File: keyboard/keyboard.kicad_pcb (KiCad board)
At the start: 2 copper layers, 64 parts, among them J1 Conn_01x04, J2 Conn_01x04, SW1 SW_Push, SW10 SW_Push, SW11 SW_Push, SW12 SW_Push, SW13 SW_Push, SW14 SW_Push, SW15 SW_Push, SW16 SW_Push, SW17 SW_Push, SW18 SW_Push, SW19 SW_Push, SW2 SW_Push, SW20 SW_Push, SW21 SW_Push, SW3 SW_Push, SW4 SW_Push, SW5 SW_Push, SW6 SW_Push, SW7 SW_Push, SW8 SW_Push, SW9 SW_Push, U1 AP2127K-3.3, U2 USBLC6-2SC6, U3 STM32F072CBTx

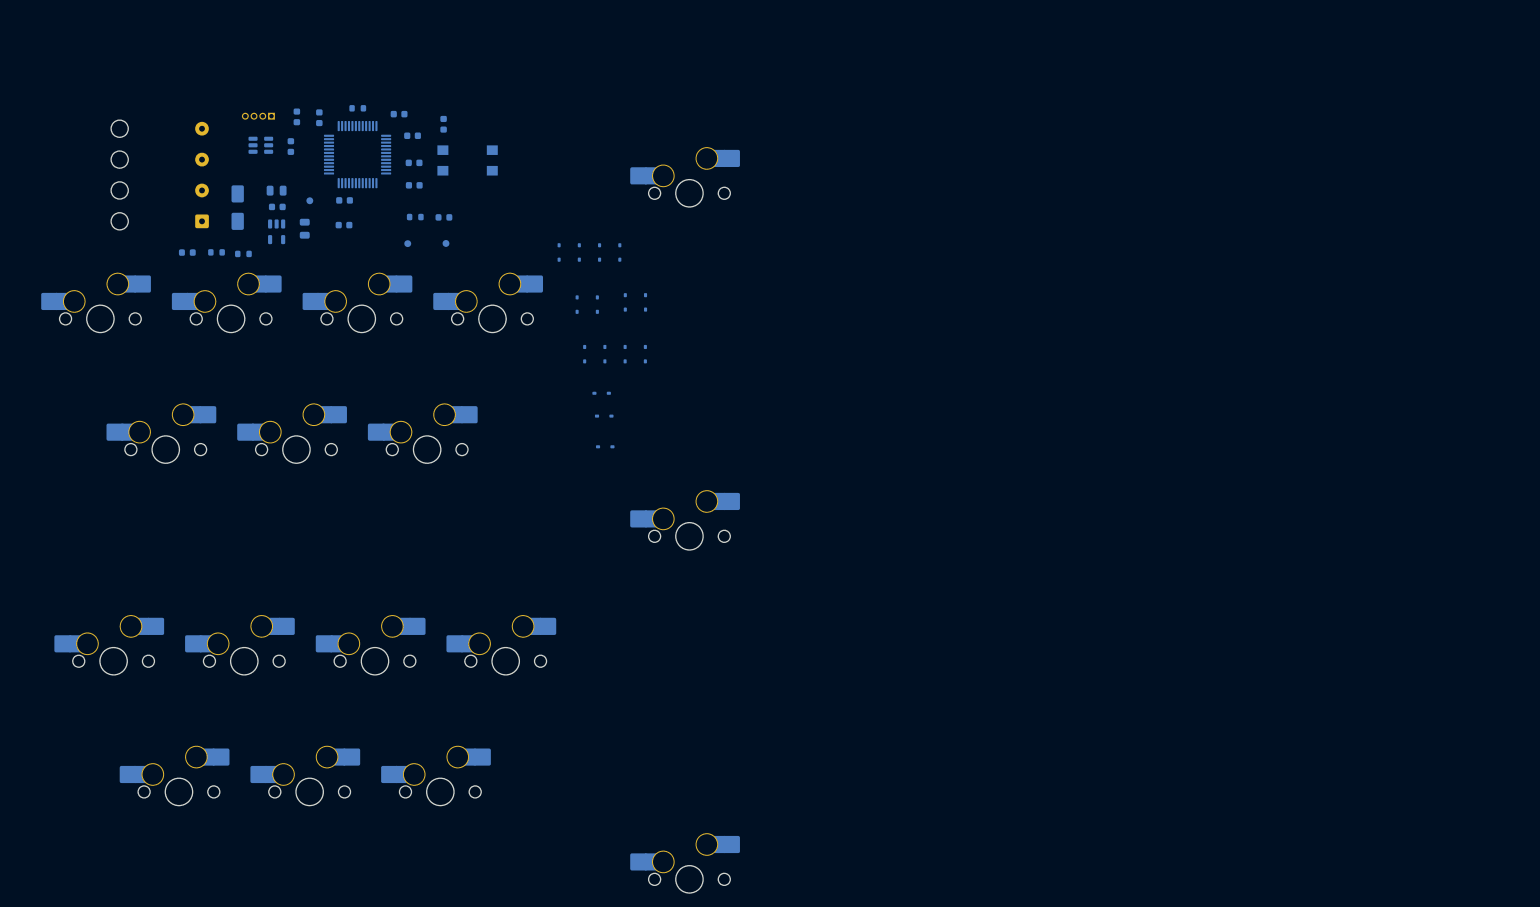
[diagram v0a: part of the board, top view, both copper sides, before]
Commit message: Key layout according to TB drawing.
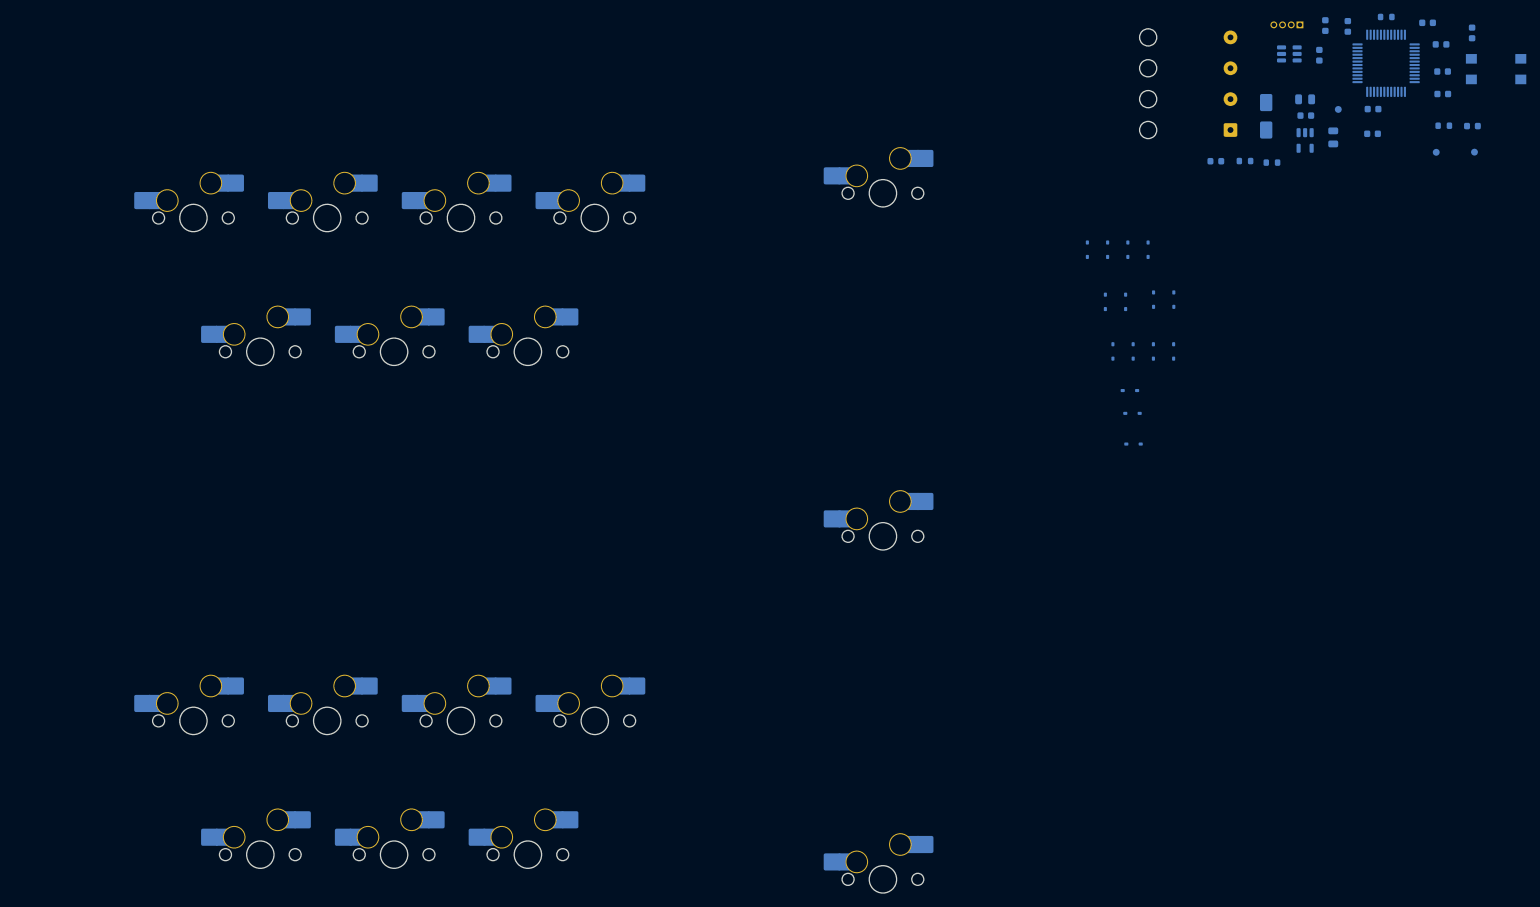
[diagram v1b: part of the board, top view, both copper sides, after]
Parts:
- moved C1 150.5 mm to (248.1, 24.9)
- moved C11 150.5 mm to (266.1, 30.5)
- moved C13 150.5 mm to (249.0, 20.6)
- moved C6 150.5 mm to (265.9, 23.3)
- moved C9 150.5 mm to (255.9, 36.3)
- moved D1 150.5 mm to (240.4, 33.8)
- moved D2 150.5 mm to (233.0, 40.3)
- moved D3 150.5 mm to (270.4, 35.2)
- moved R2 150.5 mm to (237.3, 40.3)
- moved R4 150.5 mm to (257.9, 19.3)
- moved TP1 150.5 mm to (270.7, 39.0)
- moved U2 150.5 mm to (243.7, 24.7)
- moved C10 150.5 mm to (266.1, 27.2)
- moved C12 150.5 mm to (252.3, 20.7)
- moved C2 150.5 mm to (246.0, 31.3)
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
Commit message: Added board outlines 12mm from key switch centres.
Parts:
- moved C1 149.2 mm to (114.0, 90.1)
- moved C11 149.2 mm to (131.9, 95.8)
- moved C13 149.2 mm to (114.8, 85.8)
- moved C6 149.2 mm to (131.7, 88.5)
- moved C9 149.2 mm to (121.7, 101.5)
- moved D1 149.2 mm to (106.2, 99.0)
- moved D2 149.2 mm to (98.9, 105.5)
- moved D3 149.2 mm to (136.3, 100.4)
- moved R2 149.2 mm to (103.1, 105.5)
- moved R4 149.2 mm to (123.7, 84.5)
- moved TP1 149.2 mm to (136.6, 104.2)
- moved U2 149.2 mm to (109.6, 89.9)
- moved C10 149.2 mm to (131.9, 92.5)
- moved C12 149.2 mm to (118.1, 85.9)
- moved C2 149.2 mm to (111.9, 96.5)
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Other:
- board outline added: 166.5 x 124 mm

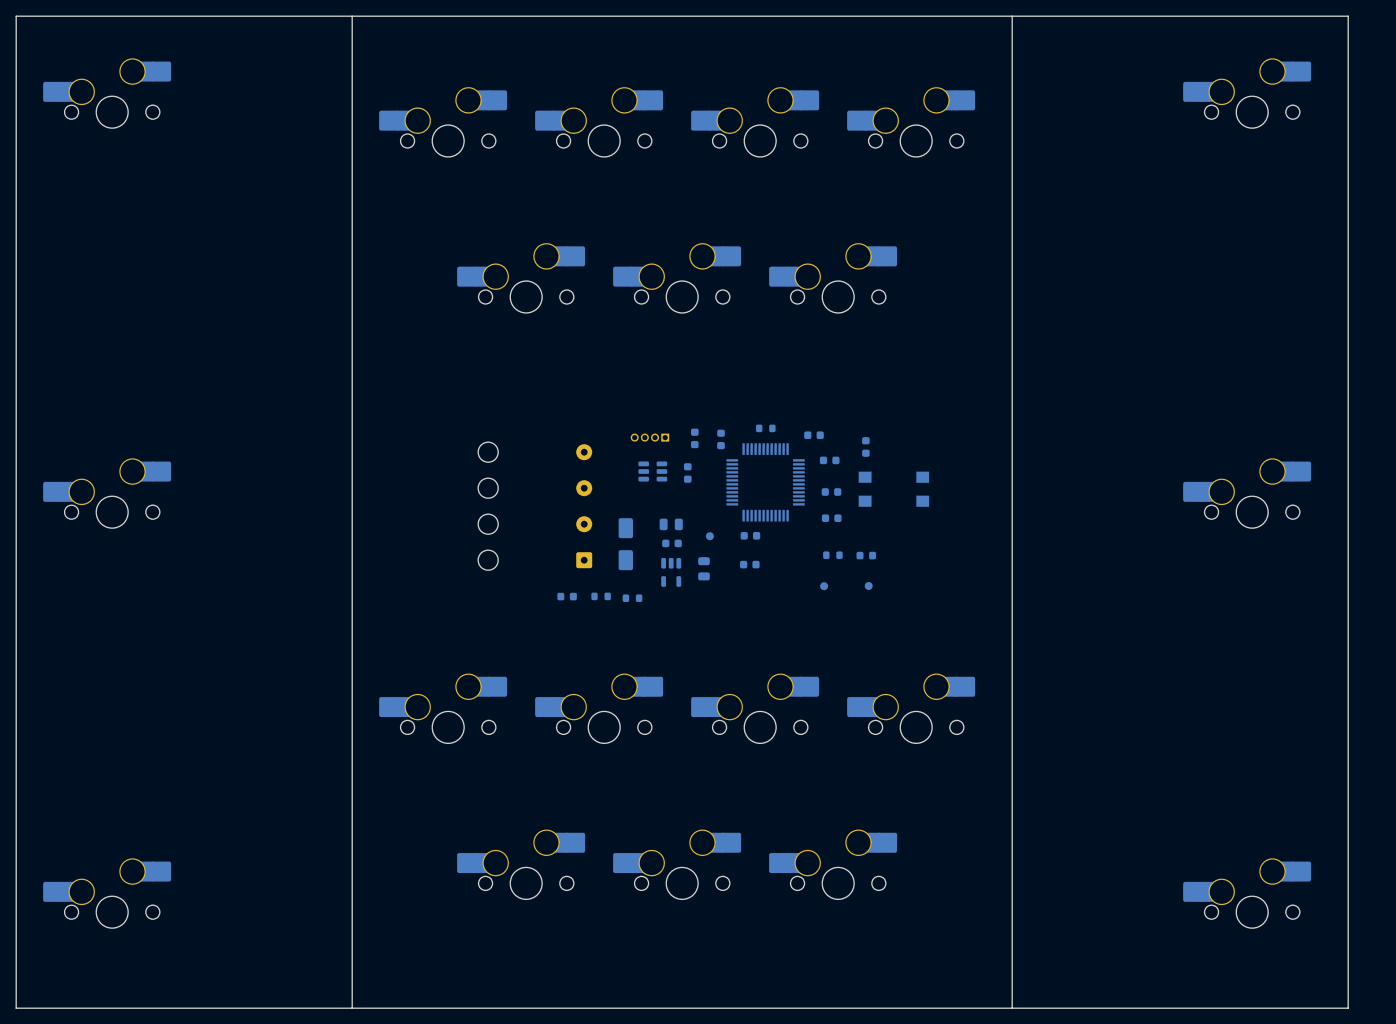
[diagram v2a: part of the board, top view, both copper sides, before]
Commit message: Added connector cutout and V-groove for cut. Moved dimensions onto user drawings layer.
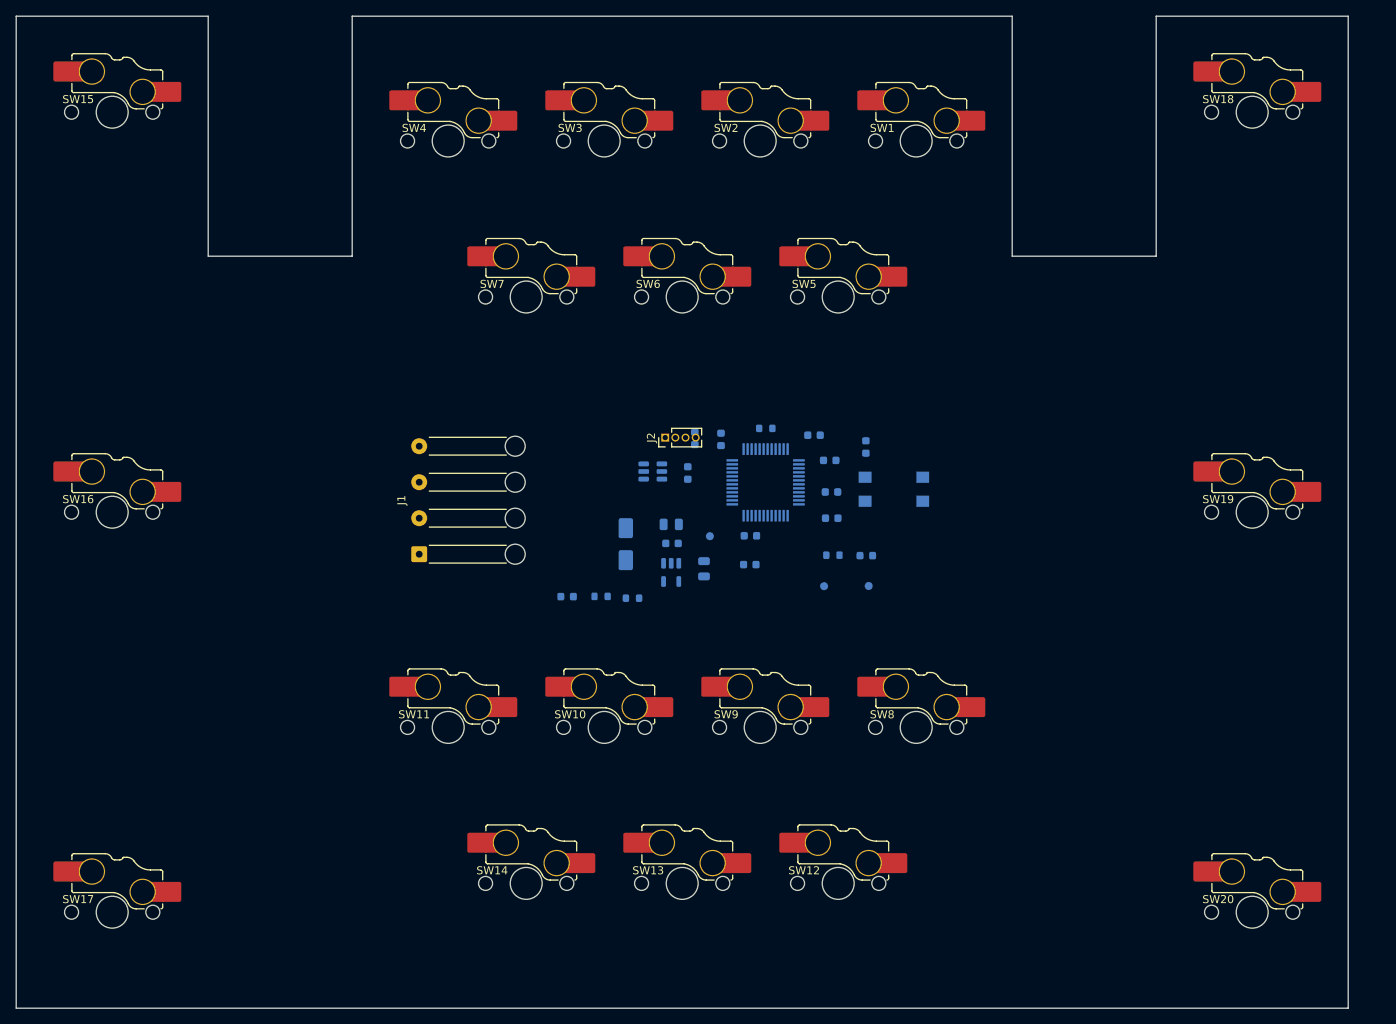
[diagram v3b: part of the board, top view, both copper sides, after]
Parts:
- J1, J2, SW1, SW10, SW11, SW12, SW13, SW14, SW15, SW16, SW17, SW18, SW19, SW2, SW20, SW3, SW4, SW5, SW6, SW7, SW8, SW9: moved to F.Cu
- moved J1 20.6 mm to (80.4, 100.2)
- turned SW1 to 0 degrees
- turned SW10 to 0 degrees
- turned SW11 to 0 degrees
- turned SW12 to 0 degrees
- turned SW13 to 0 degrees
- turned SW14 to 0 degrees
- turned SW15 to 0 degrees
- turned SW16 to 0 degrees
- turned SW17 to 0 degrees
- turned SW18 to 0 degrees
- turned SW19 to 0 degrees
- turned SW2 to 0 degrees
- turned SW20 to 0 degrees
- turned SW3 to 0 degrees
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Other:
- outline, holes or cut-outs redrawn

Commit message: Some mounting holes.
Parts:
- added REF**: MountingHole_2.2mm_M2, MountingHole:MountingHole_2.2mm_M2, F.Cu at (159.5, 152.0)
- added REF**: MountingHole_2.2mm_M2, MountingHole:MountingHole_2.2mm_M2, F.Cu at (67.0, 68.0)
- added REF**: MountingHole_2.2mm_M2, MountingHole:MountingHole_2.2mm_M2, F.Cu at (193.5, 36.0)
- added REF**: MountingHole_2.2mm_M2, MountingHole:MountingHole_2.2mm_M2, F.Cu at (77.0, 38.0)
- added REF**: MountingHole_2.2mm_M2, MountingHole:MountingHole_2.2mm_M2, F.Cu at (159.5, 68.0)
- added REF**: MountingHole_2.2mm_M2, MountingHole:MountingHole_2.2mm_M2, F.Cu at (77.0, 152.0)
- added REF**: MountingHole_2.2mm_M2, MountingHole:MountingHole_2.2mm_M2, F.Cu at (67.0, 152.0)
- added REF**: MountingHole_2.2mm_M2, MountingHole:MountingHole_2.2mm_M2, F.Cu at (159.5, 110.0)
- added REF**: MountingHole_2.2mm_M2, MountingHole:MountingHole_2.2mm_M2, F.Cu at (149.5, 68.0)
- added REF**: MountingHole_2.2mm_M2, MountingHole:MountingHole_2.2mm_M2, F.Cu at (77.0, 110.0)
- added REF**: MountingHole_2.2mm_M2, MountingHole:MountingHole_2.2mm_M2, F.Cu at (193.5, 154.0)
- added REF**: MountingHole_2.2mm_M2, MountingHole:MountingHole_2.2mm_M2, F.Cu at (149.5, 152.0)
- added REF**: MountingHole_2.2mm_M2, MountingHole:MountingHole_2.2mm_M2, F.Cu at (33.0, 36.0)
- added REF**: MountingHole_2.2mm_M2, MountingHole:MountingHole_2.2mm_M2, F.Cu at (149.5, 38.0)
- added REF**: MountingHole_2.2mm_M2, MountingHole:MountingHole_2.2mm_M2, F.Cu at (67.0, 110.0)
- added REF**: MountingHole_2.2mm_M2, MountingHole:MountingHole_2.2mm_M2, F.Cu at (33.0, 154.0)
- added REF**: MountingHole_2.2mm_M2, MountingHole:MountingHole_2.2mm_M2, F.Cu at (149.5, 110.0)
- added REF**: MountingHole_2.2mm_M2, MountingHole:MountingHole_2.2mm_M2, F.Cu at (77.0, 68.0)
- J1, J2: moved to B.Cu
- moved J1 15.3 mm to (95.6, 101.2)
- moved J2 4.18 mm to (107.0, 85.0), turned to -90 degrees

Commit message: Some switch traces.
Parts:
- SW1, SW10, SW11, SW12, SW13, SW14, SW15, SW16, SW17, SW18, SW19, SW2, SW20, SW3, SW4, SW5, SW6, SW7, SW8, SW9: moved to B.Cu
- moved D14 127.6 mm to (111.5, 128.5), turned to 90 degrees
- moved D17 122.1 mm to (121.5, 148.0), turned to 90 degrees
- moved D16 108.8 mm to (141.0, 148.0), turned to 90 degrees
- moved D13 108.4 mm to (131.0, 128.5), turned to 90 degrees
- moved D7 105.0 mm to (119.0, 40.0)
- moved D15 103.9 mm to (160.5, 148.0), turned to 90 degrees
- moved D10 102.4 mm to (121.5, 60.5)
- moved D18 98.7 mm to (127.5, 113.0), turned to 90 degrees
- moved D12 90.6 mm to (150.5, 128.5), turned to 90 degrees
- moved D6 90.2 mm to (131.0, 40.0)
- moved D11 88.7 mm to (170.0, 128.5), turned to 90 degrees
- moved D9 78.9 mm to (141.0, 60.5)
- moved D5 68.0 mm to (150.5, 40.0)
- moved D8 56.4 mm to (160.5, 60.5)
- moved D4 46.2 mm to (170.0, 40.0)
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- renumbered REF** to ?
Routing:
- net Net-(D18-A): track 0.00 -> 235.2 mm, vias 0 -> 1
- net /COL3: track 0.00 -> 226.0 mm, vias 0 -> 1
- net /ROW2: track 0.00 -> 81.7 mm
- net /COL1: track 0.00 -> 56.8 mm, vias 0 -> 5
- net /ROW3: track 0.00 -> 54.6 mm
- net /ROW1: track 0.00 -> 54.4 mm
- net /ROW0: track 0.00 -> 51.0 mm
- net /COL0: track 0.00 -> 50.2 mm, vias 0 -> 3
- net /COL2: track 0.00 -> 29.0 mm, vias 0 -> 3
- net Net-(D7-A): track 0.00 -> 11.0 mm
- net Net-(D6-A): track 0.00 -> 7.07 mm
- net Net-(D5-A): track 0.00 -> 7.07 mm
- net Net-(D4-A): track 0.00 -> 7.07 mm
- net Net-(D14-A): track 0.00 -> 6.15 mm
- net Net-(D13-A): track 0.00 -> 6.15 mm
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
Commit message: Some routing.
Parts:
- removed the ? at (194.5, 154.0)
- removed the ? at (102.0, 70.0)
- removed the ? at (228.5, 38.0)
- removed the ? at (194.5, 70.0)
- removed the ? at (102.0, 154.0)
- removed the ? at (194.5, 112.0)
- removed the ? at (184.5, 70.0)
- removed the ? at (228.5, 156.0)
- removed the ? at (102.0, 112.0)
- removed the ? at (112.0, 70.0)
- removed J1: Conn_01x04, Connector_Wire:SolderWire-0.25sqmm_1x04_P4.5mm_D0.65mm_OD2mm_Relief
- removed SW18, SW19, SW20: SW_Push, PCM_marbastlib-mx:SW_MX_HS_KS-2P02B01-01_1.5u
- added +5V: SolderWirePad_1x01_SMD_1.5x3mm, Connector_Wire:SolderWirePad_1x01_SMD_1.5x3mm, B.Cu at (139.0, 92.5)
- added ?: MountingHole_2.2mm_M2, MountingHole:MountingHole_2.2mm_M2, F.Cu at (128.2, 93.5)
- added ?: MountingHole_2.2mm_M2, MountingHole:MountingHole_2.2mm_M2, F.Cu at (128.2, 89.2)
- added ?: MountingHole_2.2mm_M2, MountingHole:MountingHole_2.2mm_M2, F.Cu at (98.5, 109.2)
- added ?: MountingHole_2.2mm_M2, MountingHole:MountingHole_2.2mm_M2, F.Cu at (104.0, 38.0)
- added ?: MountingHole_2.2mm_M2, MountingHole:MountingHole_2.2mm_M2, F.Cu at (98.5, 113.5)
- added ?: MountingHole_2.2mm_M2, MountingHole:MountingHole_2.2mm_M2, F.Cu at (104.0, 156.0)
- added ?: MountingHole_2.2mm_M2, MountingHole:MountingHole_2.2mm_M2, F.Cu at (128.2, 103.2)
- added ?: MountingHole_2.2mm_M2, MountingHole:MountingHole_2.2mm_M2, F.Cu at (128.2, 99.0)
- added COL3: SolderWirePad_1x01_SMD_1.5x3mm, Connector_Wire:SolderWirePad_1x01_SMD_1.5x3mm, B.Cu at (90.5, 110.2)
- added COL3: SolderWirePad_1x01_SMD_1.5x3mm, Connector_Wire:SolderWirePad_1x01_SMD_1.5x3mm, B.Cu at (136.2, 100.0)
- added D+_IN: SolderWirePad_1x01_SMD_1.5x3mm, Connector_Wire:SolderWirePad_1x01_SMD_1.5x3mm, B.Cu at (139.0, 88.0)
- added D_-IN: SolderWirePad_1x01_SMD_1.5x3mm, Connector_Wire:SolderWirePad_1x01_SMD_1.5x3mm, B.Cu at (139.0, 90.2)
- added GND: SolderWirePad_1x01_SMD_1.5x3mm, Connector_Wire:SolderWirePad_1x01_SMD_1.5x3mm, B.Cu at (139.0, 94.8)
- added SB_1: SolderWirePad_1x01_SMD_1.5x3mm, Connector_Wire:SolderWirePad_1x01_SMD_1.5x3mm, B.Cu at (136.2, 102.2)
- added SB_1: SolderWirePad_1x01_SMD_1.5x3mm, Connector_Wire:SolderWirePad_1x01_SMD_1.5x3mm, B.Cu at (90.5, 112.5)
- moved D18 41.8 mm to (168.8, 106.0), turned to -90 degrees
- moved C5 19.5 mm to (176.0, 104.2), turned to 180 degrees
- moved C7 18.7 mm to (172.5, 84.2)
- moved ? 18.0 mm to (86.0, 38.0)
- moved ? 18.0 mm to (86.0, 156.0)
- moved SW15 18.0 mm to (95.0, 47.0)
- moved SW16 18.0 mm to (95.0, 97.0)
- moved SW17 18.0 mm to (95.0, 147.0)
- moved C8 13.2 mm to (165.2, 96.8)
- moved J2 12.8 mm to (156.0, 85.0), turned to 0 degrees
- moved TP3 11.6 mm to (155.8, 101.8), turned to 0 degrees
- moved SW21 11.4 mm to (180.8, 100.8), turned to 90 degrees
- moved D3 10.6 mm to (162.5, 101.8)
- moved R3 9.93 mm to (159.0, 101.8)
- moved U1 9.55 mm to (156.8, 96.5), turned to 0 degrees
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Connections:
- net Net-(D18-A) renamed /SB_1
- SW15 pad 2: /COL3 -> Net-(J3-Pin_2)
- SW16 pad 2: /COL3 -> Net-(J3-Pin_2)
- SW17 pad 2: /COL3 -> Net-(J3-Pin_2)
- U3 pad 11: /COL2 -> unconnected-(U3-PA1-Pad11)
- U3 pad 12: /COL1 -> unconnected-(U3-PA2-Pad12)
- U3 pad 13: /COL0 -> unconnected-(U3-PA3-Pad13)
- U3 pad 14: /ROW0 -> unconnected-(U3-PA4-Pad14)
- U3 pad 15: /ROW1 -> /ROW2
- U3 pad 16: /ROW2 -> /ROW3
- U3 pad 17: /ROW3 -> unconnected-(U3-PA7-Pad17)
- U3 pad 38: unconnected-(U3-PA15-Pad38) -> /COL2
- U3 pad 40: unconnected-(U3-PB4-Pad40) -> /COL1
- U3 pad 42: unconnected-(U3-PB6-Pad42) -> /ROW1
- U3 pad 43: unconnected-(U3-PB7-Pad43) -> /COL0
- U3 pad 46: unconnected-(U3-PB9-Pad46) -> /ROW0
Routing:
- net /COL2: track 29.0 -> 159.4 mm, vias 3 -> 5
- net /COL1: track 56.8 -> 185.8 mm
- net /SB_1: track 235.2 -> 141.1 mm, vias 1 -> 0
- net /ROW3: track 54.6 -> 136.3 mm, vias 0 -> 2
- net /ROW0: track 51.0 -> 123.4 mm
- net /ROW1: track 54.4 -> 121.3 mm
- net /COL0: track 50.2 -> 109.5 mm, vias 3 -> 2
- net /ROW2: track 81.7 -> 125.3 mm
- net /NRST: track 0.00 -> 27.1 mm
- net /SWCLK: track 0.00 -> 12.4 mm
- net /COL3: track 226.0 -> 215.9 mm, vias 1 -> 2
- net /SWDIO: track 0.00 -> 8.70 mm
- net /BOOT: track 0.00 -> 4.66 mm
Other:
- board size 166.5 x 124 mm -> 106.5 x 124 mm
